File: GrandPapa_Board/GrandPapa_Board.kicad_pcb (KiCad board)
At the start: 4 copper layers, 82 x 82 mm, 95 parts, among them J1 3.7V LiPo Single Cell, J11 Dupont 01x04_Male, J2 HARWIN_ROCKET, J3 Dupont_GPS, J4 HARWIN_MINISENSOR, J5 Dupont_Logger, J6 Conn_02x06, J7 HARWIN_KALMAN, U1 MCP1642B-50I/MS, U10 MCP2515-I/P, U2 BD9E302EFJ, U3 MCP73871T-1CCI/ML, U4 INA180, U5 FPF2124, U6 INA180, U7 MCP2562-E/SN, U8 MCP2562-E/SN, U9 PIC18F26K83, Y1 12MHz

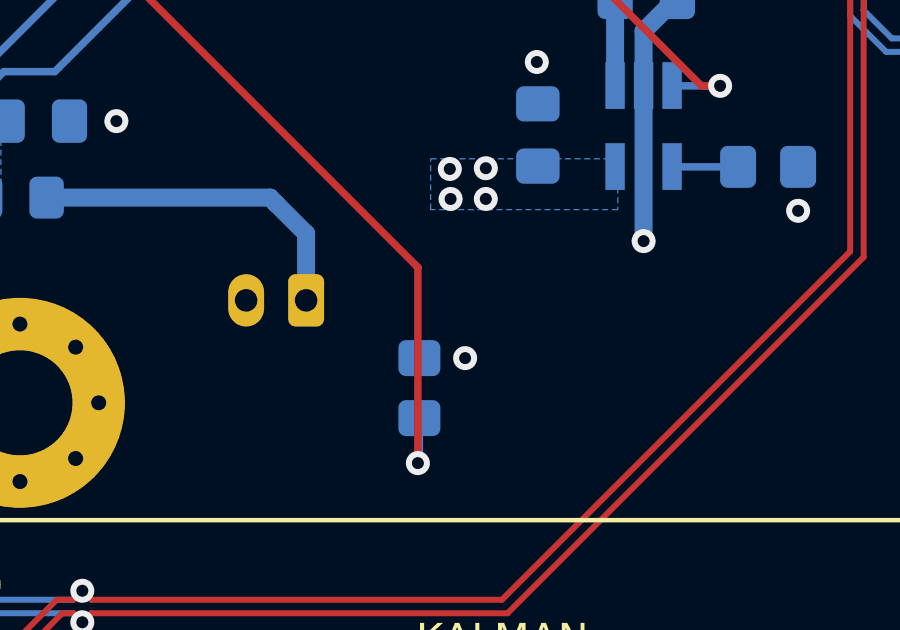
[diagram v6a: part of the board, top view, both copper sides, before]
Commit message: Add R28 to fix thermal shdn; Add BOM and thermistor calc sheets
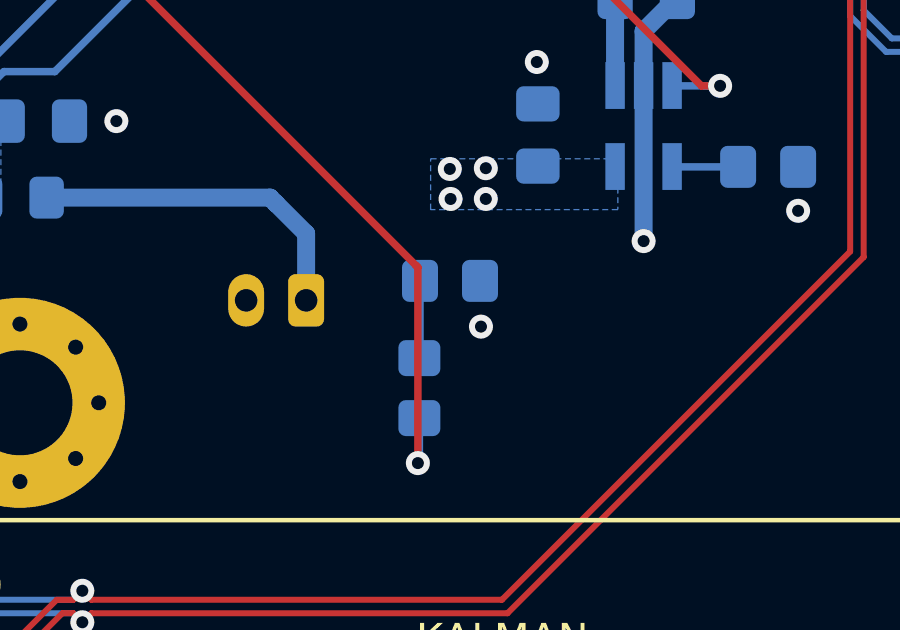
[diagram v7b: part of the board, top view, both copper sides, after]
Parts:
- added R28: 2.5kR, Resistor_SMD:R_0805_2012Metric_Pad1.20x1.40mm_HandSolder, B.Cu at (173.1, 122.1)
- J6: value Conn_02x06 -> PROG Header
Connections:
- TH1 pad 2: GND -> Net-(TH1-Pad2)
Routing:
- net Net-(TH1-Pad2): track 0.00 -> 2.58 mm
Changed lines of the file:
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@@
   (net 48 "Net-(R23-Pad1)")
   (net 49 "Net-(R26-Pad1)")
-  (net 50 "Net-(TH1-Pad1)")
+  (net 50 "Net-(TH1-Pad2)")
   (net 51 "Net-(TP7-Pad1)")
   (net 52 "unconnected-(U1-Pad2)")
@@
   (net 80 "/MCU and CAN Controllers/CANH_ROCKET")
   (net 81 "/MCU and CAN Controllers/CANL_ROCKET")
+  (net 82 "Net-(U3-Pad5)")
   (footprint "Capacitor_SMD:C_0805_2012Metric_Pad1.18x1.45mm_HandSolder" (layer "F.Cu")
     (at 153.489 68.3718 -90)
@@
       (effects (font (size 1 1) (thickness 0.15)))
     )
-    (fp_text value "Conn_02x06" (at -3.175 5.71) (layer "F.Fab")
+    (fp_text value "PROG Header" (at -3.175 5.71) (layer "F.Fab")
       (effects (font (size 1 1) (thickness 0.15)))
     )
@@
       (net 10 "+4.5V") (pinfunction "PROG2") (pintype "input"))
     (pad "5" smd roundrect (at -1.9375 -1) (size 0.825 0.25) (layers "B.Cu" "B.Paste" "B.Mask") (roundrect_rratio 0.25)
-      (net 50 "Net-(TH1-Pad1)") (pinfunction "THERM") (pintype "bidirectional"))
+      (net 82 "Net-(U3-Pad5)") (pinfunction "THERM") (pintype "bidirectional"))
     (pad "6" smd roundrect (at -1 -1.9375) (size 0.25 0.825) (layers "B.Cu" "B.Paste" "B.Mask") (roundrect_rratio 0.25)
       (net 46 "/Battery Charging/BATT_CHARGER_PG") (pinfunction "~{PG}") (pintype "open_collector"))
@@
     )
   )
+  (footprint "Resistor_SMD:R_0805_2012Metric_Pad1.20x1.40mm_HandSolder" (layer "B.Cu")
+    (at 173.085 122.0978)
+    (descr "Resistor SMD 0805 (2012 Metric), square (rectangular) end terminal, IPC_7351 nominal with elongated pad for handsoldering. (Body size source: IPC-SM-782 page 72, https://www.pcb-3d.com/wordpress/wp-content/uploads/ipc-sm-782a_amendment_1_and_2.pdf), generated with kicad-footprint-generator")
+    (tags "resistor handsolder")
+    (property "Sheetfile" "grandpapa_Charge.kicad_sch")
+    (property "Sheetname" "Battery Charging")
+    (attr smd)
+    (fp_text reference "R28" (at 3.572 0) (layer "B.SilkS")
+      (effects (font (size 1 1) (thickness 0.15)) (justify mirror))
+    )
+    (fp_text value "2.5kR" (at 0 -1.65) (layer "B.Fab")
+      (effects (font (size 1 1) (thickness 0.15)) (justify mirror))
+    )
+    (fp_text user "${REFERENCE}" (at 0 0) (layer "B.Fab")
+      (effects (font (size 0.5 0.5) (thickness 0.08)) (justify mirror))
+    )
+    (fp_line (start -0.227064 0.735) (end 0.227064 0.735) (layer "B.SilkS") (width 0.12))
+    (fp_line (start -0.227064 -0.735) (end 0.227064 -0.735) (layer "B.SilkS") (width 0.12))
+    (fp_line (start -1.85 -0.95) (end -1.85 0.95) (layer "B.CrtYd") (width 0.05))
+    (fp_line (start -1.85 0.95) (end 1.85 0.95) (layer "B.CrtYd") (width 0.05))
+    (fp_line (start 1.85 0.95) (end 1.85 -0.95) (layer "B.CrtYd") (width 0.05))
+    (fp_line (start 1.85 -0.95) (end -1.85 -0.95) (layer "B.CrtYd") (width 0.05))
+    (fp_line (start -1 0.625) (end 1 0.625) (layer "B.Fab") (width 0.1))
+    (fp_line (start 1 0.625) (end 1 -0.625) (layer "B.Fab") (width 0.1))
+    (fp_line (start 1 -0.625) (end -1 -0.625) (layer "B.Fab") (width 0.1))
+    (fp_line (start -1 -0.625) (end -1 0.625) (layer "B.Fab") (width 0.1))
+    (pad "1" smd roundrect (at -1 0) (size 1.2 1.4) (layers "B.Cu" "B.Paste" "B.Mask") (roundrect_rratio 0.208333)
+      (net 50 "Net-(TH1-Pad2)") (pintype "passive"))
+    (pad "2" smd roundrect (at 1 0) (size 1.2 1.4) (layers "B.Cu" "B.Paste" "B.Mask") (roundrect_rratio 0.208333)
+      (net 2 "GND") (pintype "passive"))
+    (model "${KICAD6_3DMODEL_DIR}/Resistor_SMD.3dshapes/R_0805_2012Metric.wrl"
+      (offset (xyz 0 0 0))
+      (scale (xyz 1 1 1))
+      (rotate (xyz 0 0 0))
+    )
+  )
   (footprint "Inductor_SMD:L_Sumida_CDMC6D28_7.25x6.5mm" (layer "B.Cu")
     (at 175.809 94.4018 180)
@@
     (fp_line (start -1 0.625) (end 1 0.625) (layer "B.Fab") (width 0.1))
     (pad "1" smd roundrect (at -1 0 90) (size 1.2 1.4) (layers "B.Cu" "B.Paste" "B.Mask") (roundrect_rratio 0.208333)
-      (net 50 "Net-(TH1-Pad1)") (pintype "passive"))
+      (net 82 "Net-(U3-Pad5)") (pintype "passive"))
     (pad "2" smd roundrect (at 1 0 90) (size 1.2 1.4) (layers "B.Cu" "B.Paste" "B.Mask") (roundrect_rratio 0.208333)
-      (net 2 "GND") (pintype "passive"))
+      (net 50 "Net-(TH1-Pad2)") (pintype "passive"))
     (model "${KICAD6_3DMODEL_DIR}/Resistor_SMD.3dshapes/R_0805_2012Metric.wrl"
       (offset (xyz 0 0 0))
@@
   (via (at 140.369 88.9518) (size 0.8) (drill 0.4) (layers "F.Cu" "B.Cu") (free) (net 2))
   (via (at 175.789 101.5468) (size 0.8) (drill 0.4) (layers "F.Cu" "B.Cu") (free) (net 2))
-  (via (at 173.589 124.6718) (size 0.8) (drill 0.4) (layers "F.Cu" "B.Cu") (free) (net 2))
+  (via (at 174.117 123.6218) (size 0.8) (drill 0.4) (layers "F.Cu" "B.Cu") (free) (net 2))
   (via (at 132.709 83.4418) (size 0.8) (drill 0.4) (layers "F.Cu" "B.Cu") (free) (net 2))
   (via (at 147.955 71.8058) (size 0.8) (drill 0.4) (layers "F.Cu" "B.Cu") (free) (net 2))
@@
   (segment (start 153.689 95.1968) (end 153.689 97.8682) (width 0.8) (layer "B.Cu") (net 48))
   (segment (start 185.254 82.2218) (end 182.489 82.2218) (width 0.25) (layer "B.Cu") (net 49))
-  (segment (start 147.639 114.3976) (end 147.639 111.7968) (width 0.25) (layer "F.Cu") (net 50))
-  (segment (start 148.9542 115.7128) (end 147.639 114.3976) (width 0.25) (layer "F.Cu") (net 50))
-  (segment (start 148.488511 110.947289) (end 161.314489 110.947289) (width 0.25) (layer "F.Cu") (net 50))
-  (segment (start 172.014 121.6468) (end 171.9515 121.5843) (width 0.25) (layer "F.Cu") (net 50))
-  (segment (start 161.314489 110.947289) (end 171.9515 121.5843) (width 0.25) (layer "F.Cu") (net 50))
-  (segment (start 172.014 128.1718) (end 172.014 121.6468) (width 0.25) (layer "F.Cu") (net 50))
-  (segment (start 147.639 111.7968) (end 148.488511 110.947289) (width 0.25) (layer "F.Cu") (net 50))
-  (via (at 172.014 128.1718) (size 0.8) (drill 0.4) (layers "F.Cu" "B.Cu") (net 50))
-  (via (at 148.9542 115.7128) (size 0.8) (drill 0.4) (layers "F.Cu" "B.Cu") (net 50))
-  (segment (start 172.064 128.1218) (end 172.014 128.1718) (width 0.25) (layer "B.Cu") (net 50))
-  (segment (start 148.9542 115.7128) (end 149.2182 115.9768) (width 0.25) (layer "B.Cu") (net 50))
-  (segment (start 172.064 126.6718) (end 172.064 128.1218) (width 0.25) (layer "B.Cu") (net 50))
-  (segment (start 149.2182 115.9768) (end 150.5065 115.9768) (width 0.25) (layer "B.Cu") (net 50))
+  (segment (start 172.085 122.0978) (end 172.085 124.6508) (width 0.25) (layer "B.Cu") (net 50))
+  (segment (start 172.085 124.6508) (end 172.064 124.6718) (width 0.25) (layer "B.Cu") (net 50))
   (segment (start 174.487434 66.4218) (end 181.939 66.4218) (width 0.25) (layer "F.Cu") (net 51))
   (segment (start 168.472435 72.4368) (end 174.487434 66.4218) (width 0.25) (layer "F.Cu") (net 51))
@@
   (segment (start 144.538401 66.316399) (end 145.3134 65.5414) (width 0.2) (layer "B.Cu") (net 81))
   (segment (start 180.174411 73.046801) (end 181.068199 73.046801) (width 0.2) (layer "B.Cu") (net 81))
+  (segment (start 147.639 114.3976) (end 147.639 111.7968) (width 0.25) (layer "F.Cu") (net 82))
+  (segment (start 148.9542 115.7128) (end 147.639 114.3976) (width 0.25) (layer "F.Cu") (net 82))
+  (segment (start 148.488511 110.947289) (end 161.314489 110.947289) (width 0.25) (layer "F.Cu") (net 82))
+  (segment (start 172.014 121.6468) (end 171.9515 121.5843) (width 0.25) (layer "F.Cu") (net 82))
+  (segment (start 161.314489 110.947289) (end 171.9515 121.5843) (width 0.25) (layer "F.Cu") (net 82))
+  (segment (start 172.014 128.1718) (end 172.014 121.6468) (width 0.25) (layer "F.Cu") (net 82))
+  (segment (start 147.639 111.7968) (end 148.488511 110.947289) (width 0.25) (layer "F.Cu") (net 82))
+  (via (at 172.014 128.1718) (size 0.8) (drill 0.4) (layers "F.Cu" "B.Cu") (net 82))
+  (via (at 148.9542 115.7128) (size 0.8) (drill 0.4) (layers "F.Cu" "B.Cu") (net 82))
+  (segment (start 172.064 128.1218) (end 172.014 128.1718) (width 0.25) (layer "B.Cu") (net 82))
+  (segment (start 148.9542 115.7128) (end 149.2182 115.9768) (width 0.25) (layer "B.Cu") (net 82))
+  (segment (start 172.064 126.6718) (end 172.064 128.1218) (width 0.25) (layer "B.Cu") (net 82))
+  (segment (start 149.2182 115.9768) (end 150.5065 115.9768) (width 0.25) (layer "B.Cu") (net 82))
   (zone (net 2) (net_name "GND") (layer "F.Cu") (hatch edge 0.508)
     (connect_pads (clearance 0.508))

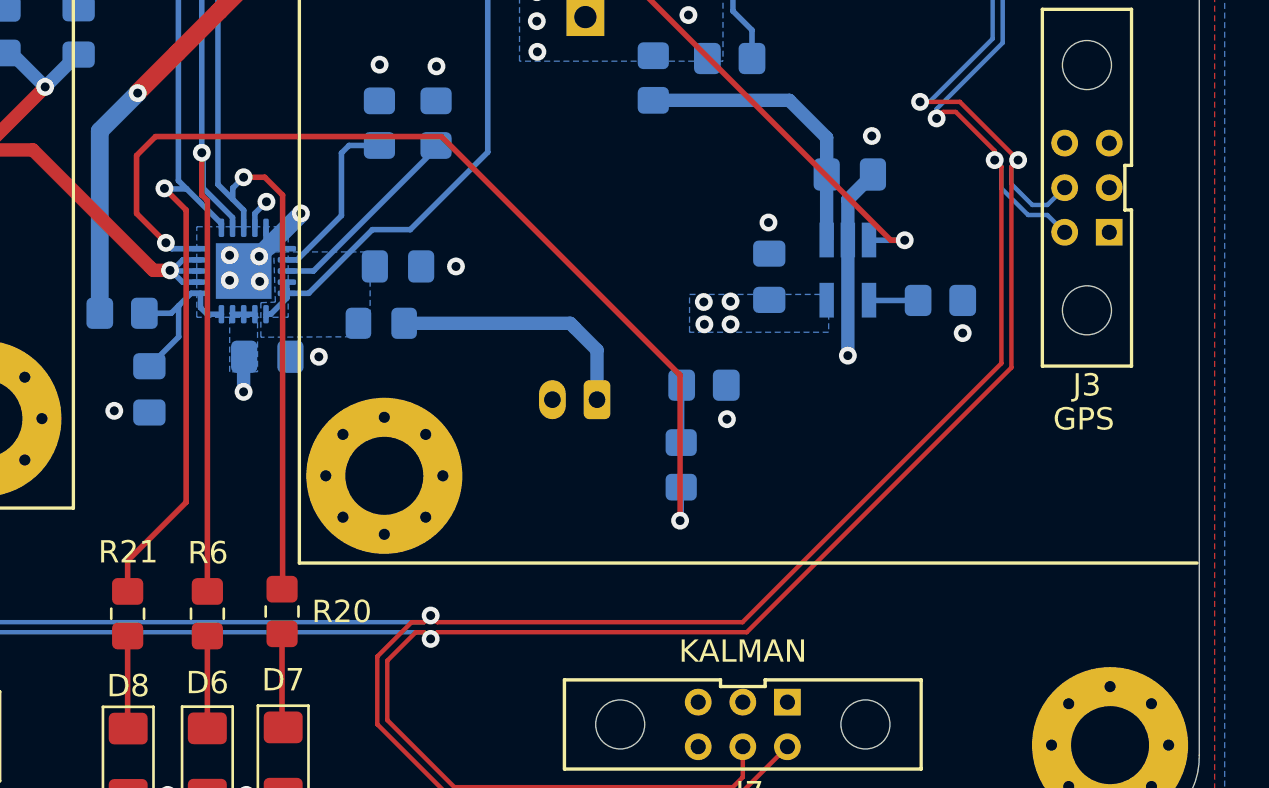
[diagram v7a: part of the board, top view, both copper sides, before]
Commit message: Add jumper to bypass thermal shutdown
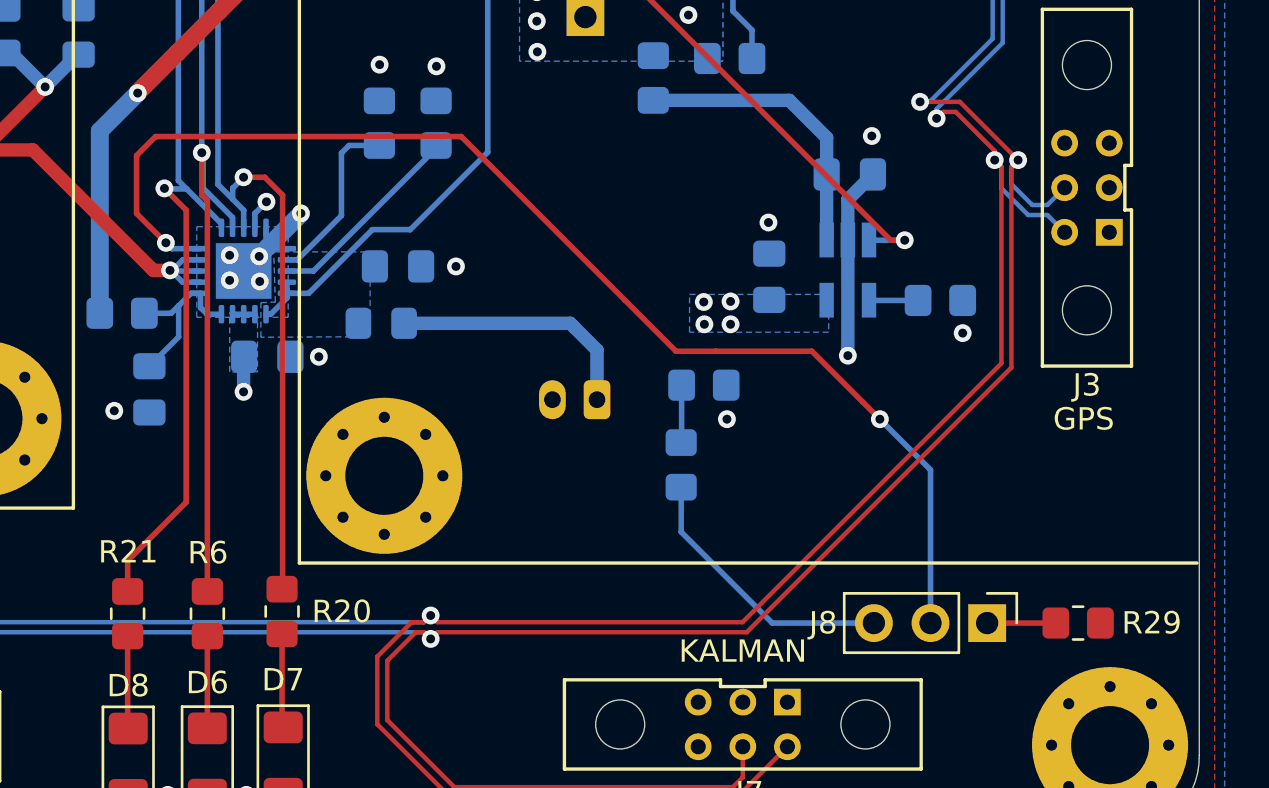
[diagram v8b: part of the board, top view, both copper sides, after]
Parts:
- added J8: Therm EN Jumper, Connector_PinHeader_2.54mm:PinHeader_1x03_P2.54mm_Vertical, F.Cu at (185.8, 132.8)
- added R29: 15kR, Resistor_SMD:R_0805_2012Metric_Pad1.20x1.40mm_HandSolder, F.Cu at (189.9, 132.8)
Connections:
- TH1 pad 1: Net-(U3-Pad5) -> Net-(TH1-Pad1)
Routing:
- net Net-(TH1-Pad1): track 0.00 -> 12.3 mm
- net Net-(U3-Pad5): track 43.3 -> 55.1 mm
- net Net-(J8-Pad1): track 0.00 -> 3.08 mm
